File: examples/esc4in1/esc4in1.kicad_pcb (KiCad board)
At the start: 4 copper layers, 44 x 43.5 mm, 87 parts, among them J1 VBAT+, J11 M1_U, J12 M1_V, J13 M1_W, J14 M2_U, J15 M2_V, J16 M2_W, J17 M3_U, J18 M3_V, J19 M3_W, J2 GND, J20 M4_U, J21 M4_V, J22 M4_W, J3 FC, Q1 CSD18540Q5B, Q10 CSD18540Q5B, Q11 CSD18540Q5B, Q12 CSD18540Q5B, Q13 CSD18540Q5B, Q14 CSD18540Q5B, Q15 CSD18540Q5B, Q16 CSD18540Q5B, Q17 CSD18540Q5B, Q18 CSD18540Q5B, Q19 CSD18540Q5B, Q2 CSD18540Q5B, Q20 CSD18540Q5B, Q21 CSD18540Q5B, Q22 CSD18540Q5B, Q23 CSD18540Q5B, Q24 CSD18540Q5B, Q3 CSD18540Q5B, Q4 CSD18540Q5B, Q5 CSD18540Q5B, Q6 CSD18540Q5B, Q7 CSD18540Q5B, Q8 CSD18540Q5B, Q9 CSD18540Q5B, U1 STSPIN32F0A, U2 STSPIN32F0A, U3 STSPIN32F0A, U4 STSPIN32F0A

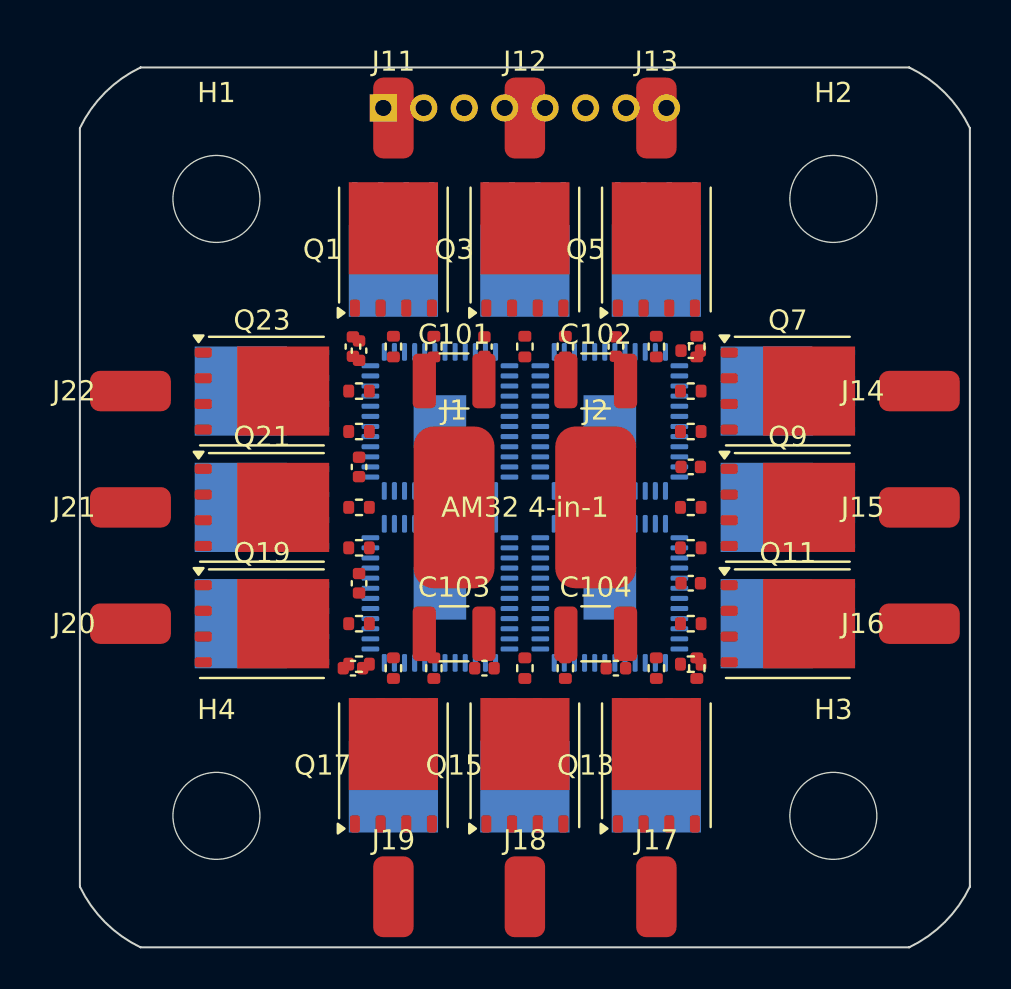
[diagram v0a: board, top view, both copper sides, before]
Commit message: Harden primitive design APIs and examples
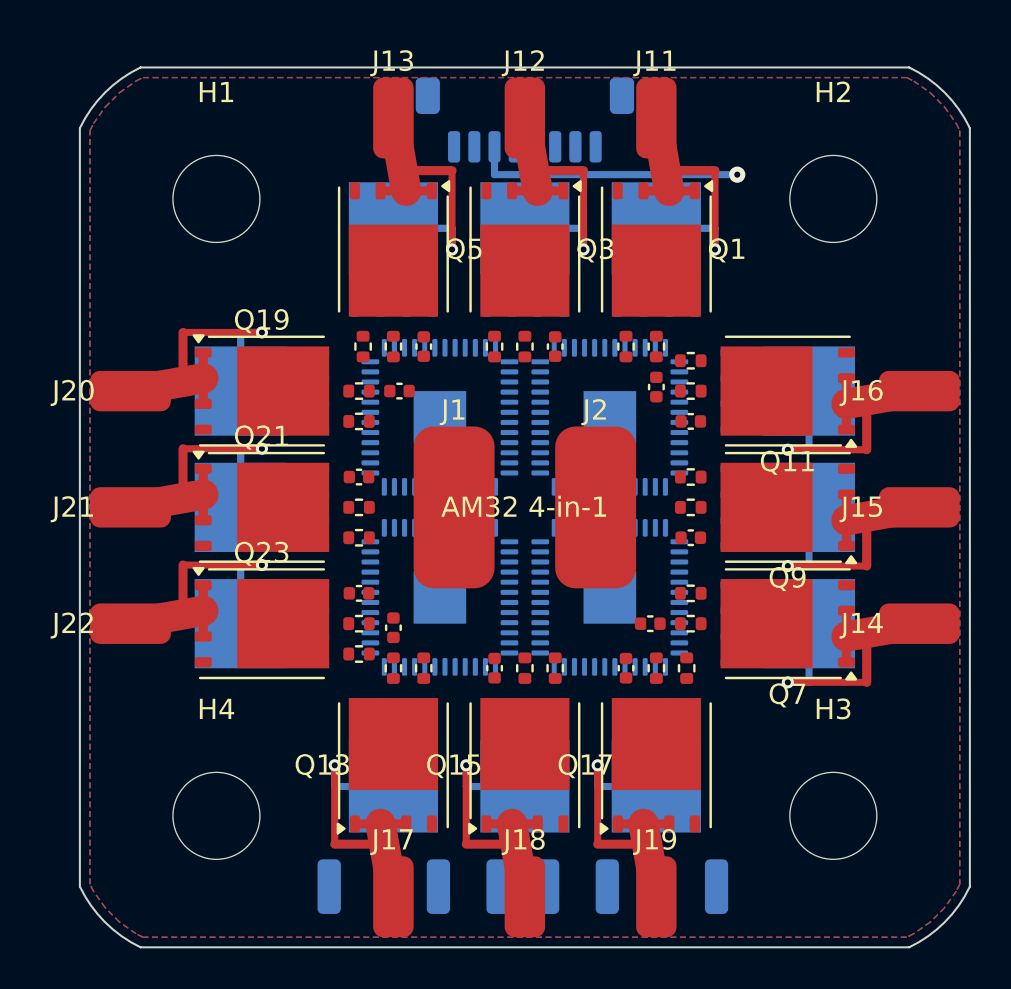
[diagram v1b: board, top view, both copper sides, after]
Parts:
- C101, C102, C103, C104: moved to B.Cu
- J3: footprint Connector_PinHeader_2.00mm:PinHeader_1x08_P2.00mm_Vertical -> Connector_JST:JST_SH_BM08B-SRSS-TB_1x08-1MP_P1.00mm_Vertical
- moved C102 25.8 mm to (19.2, 40.5)
- moved C101 25.4 mm to (13.8, 40.5)
- moved C1 15.1 mm to (28.5, 15.8), turned to 90 degrees
- moved R14 15.0 mm to (15.5, 29.7), turned to -90 degrees
- moved R6 15.0 mm to (15.5, 13.8)
- moved R17 14.5 mm to (30.0, 29.7), turned to -90 degrees
- moved R5 14.5 mm to (14.0, 13.8)
- moved C103 13.9 mm to (24.6, 40.5)
- moved C4 13.6 mm to (28.2, 27.5)
- moved C9 13.5 mm to (27.0, 29.7), turned to -90 degrees
- moved R12 13.5 mm to (30.2, 16.0)
- moved R20 13.5 mm to (13.8, 16.0), turned to 180 degrees
- moved C104 13.3 mm to (30.0, 40.5)
- moved J11 13.0 mm to (28.5, 2.50)
- moved J13 13.0 mm to (15.5, 2.50)
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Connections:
- U1 pad 10: (no net) -> +3V3
- U1 pad 48: (no net) -> +3V3
- U2 pad 10: (no net) -> +3V3
- U2 pad 48: (no net) -> +3V3
- U3 pad 10: (no net) -> +3V3
- U3 pad 48: (no net) -> +3V3
- U4 pad 10: (no net) -> +3V3
- U4 pad 48: (no net) -> +3V3
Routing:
- net M4_U: track 0.00 -> 17.3 mm, vias 0 -> 1
- net M4_W: track 0.00 -> 17.3 mm, vias 0 -> 1
- net M4_V: track 0.00 -> 17.3 mm, vias 0 -> 1
- net M3_U: track 0.00 -> 17.3 mm, vias 0 -> 1
- net M1_V: track 0.00 -> 17.3 mm, vias 0 -> 1
- net M1_U: track 0.00 -> 17.3 mm, vias 0 -> 1
- net M3_W: track 0.00 -> 17.3 mm, vias 0 -> 1
- net M3_V: track 0.00 -> 17.3 mm, vias 0 -> 1
- net M2_W: track 0.00 -> 17.3 mm, vias 0 -> 1
- net M2_V: track 0.00 -> 17.3 mm, vias 0 -> 1
- net M2_U: track 0.00 -> 17.3 mm, vias 0 -> 1
- net M1_W: track 0.00 -> 17.3 mm, vias 0 -> 1
- net VBAT: track 0.00 -> 13.4 mm, vias 0 -> 1
- added copper zone on B.Cu, net GND
- added copper zone on F.Cu, net VBAT

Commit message: Improve PCB connectivity facts and ESC reference
Use native KiCad connectivity for point and unrouted inspection, set the advisory grid to 0.1 mm, and correct the ESC example's Betaflight connector pinout and partial routing. The ESC remains a non-operable reference with 74 unrouted connections; its schematic marks missing controller support circuits.
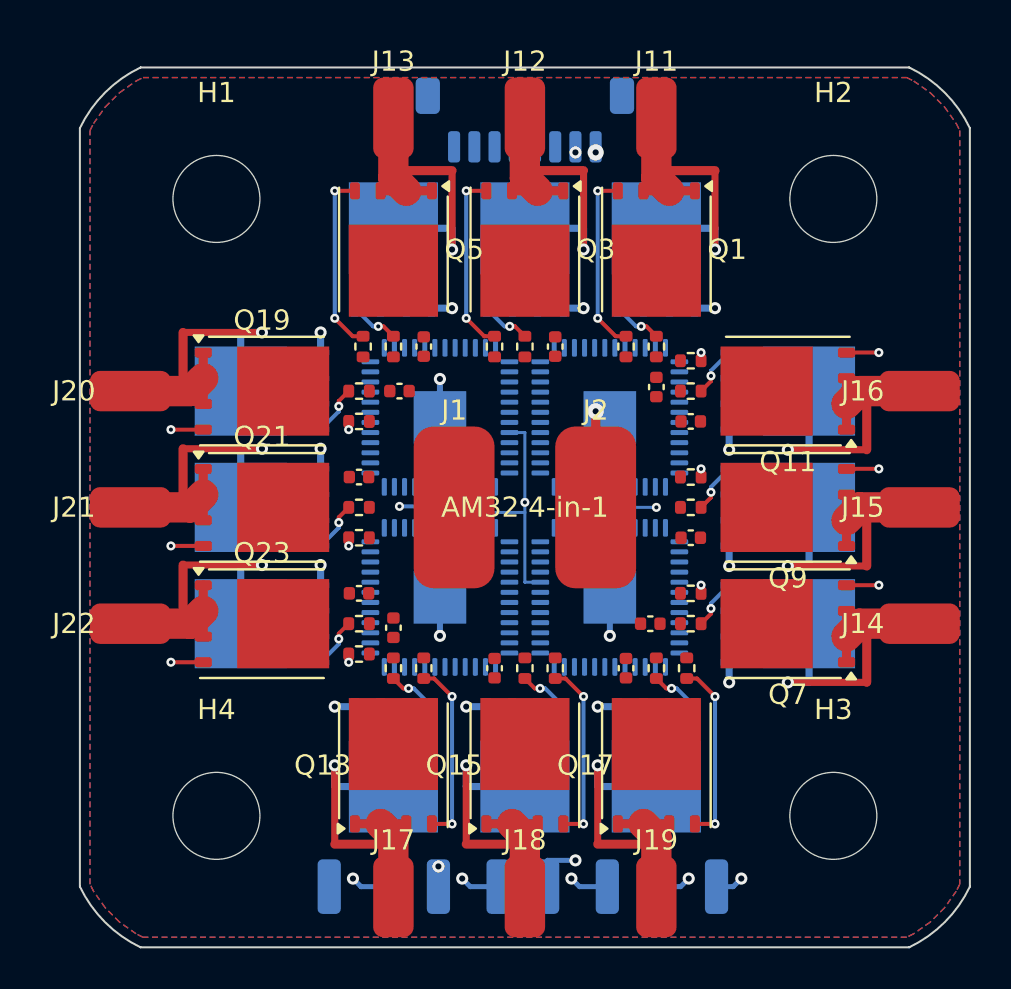
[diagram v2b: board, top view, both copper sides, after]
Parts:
- turned C101 to 180 degrees
- turned C102 to 180 degrees
- turned C103 to 180 degrees
- turned C104 to 180 degrees
- turned J3 to 180 degrees
- turned Q10 to 0 degrees
- turned Q12 to 0 degrees
- turned Q14 to -90 degrees
- turned Q16 to -90 degrees
- turned Q18 to -90 degrees
- turned Q2 to 90 degrees
- turned Q20 to 180 degrees
- turned Q22 to 180 degrees
- turned Q24 to 180 degrees
- turned Q4 to 90 degrees
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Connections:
- J3 pad 1: DSHOT1 -> VBAT
- J3 pad 2: DSHOT2 -> GND
- J3 pad 3: DSHOT3 -> (no net)
- J3 pad 4: DSHOT4 -> (no net)
- J3 pad 5: CURRENT -> DSHOT1
- J3 pad 6: VBAT -> DSHOT2
- J3 pad 7: +3V3 -> DSHOT3
- J3 pad 8: GND -> DSHOT4
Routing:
- net GND: track 0.00 -> 45.3 mm, vias 0 -> 22
- net M2_V_GH: track 0.00 -> 10.8 mm, vias 0 -> 2
- net M2_U_GH: track 0.00 -> 10.8 mm, vias 0 -> 2
- net M4_W_GH: track 0.00 -> 10.8 mm, vias 0 -> 2
- net M4_V_GH: track 0.00 -> 10.8 mm, vias 0 -> 2
- net M4_U_GH: track 0.00 -> 10.8 mm, vias 0 -> 2
- net M2_W_GH: track 0.00 -> 10.8 mm, vias 0 -> 2
- net M1_W_GH: track 0.00 -> 9.06 mm, vias 0 -> 2
- net M1_V_GH: track 0.00 -> 9.06 mm, vias 0 -> 2
- net M1_U_GH: track 0.00 -> 9.06 mm, vias 0 -> 2
- net M3_W_GH: track 0.00 -> 9.06 mm, vias 0 -> 2
- net M3_V_GH: track 0.00 -> 9.06 mm, vias 0 -> 2
- net M3_U_GH: track 0.00 -> 9.06 mm, vias 0 -> 2
- net VBAT: track 13.4 -> 9.70 mm, vias 1 -> 6
- net M3_W_GL: track 0.00 -> 2.48 mm, vias 0 -> 1
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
